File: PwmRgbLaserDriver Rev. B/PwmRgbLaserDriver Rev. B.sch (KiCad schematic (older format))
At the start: 55 parts, among them IC1 ADA4817-1ARDZ, IC2 ADA4817-1ARDZ, IC3 ADA4817-1ARDZ, J1 RED_IN, J2 15V, J3 RLO, J4 GREEN_IN, J5 GLO, J6 BLUE_IN, J7 BLO, Q1 Q_NPN_BCE, Q2 Q_NPN_BCE, Q3 Q_NPN_BCE, U1 TPS54331GDR

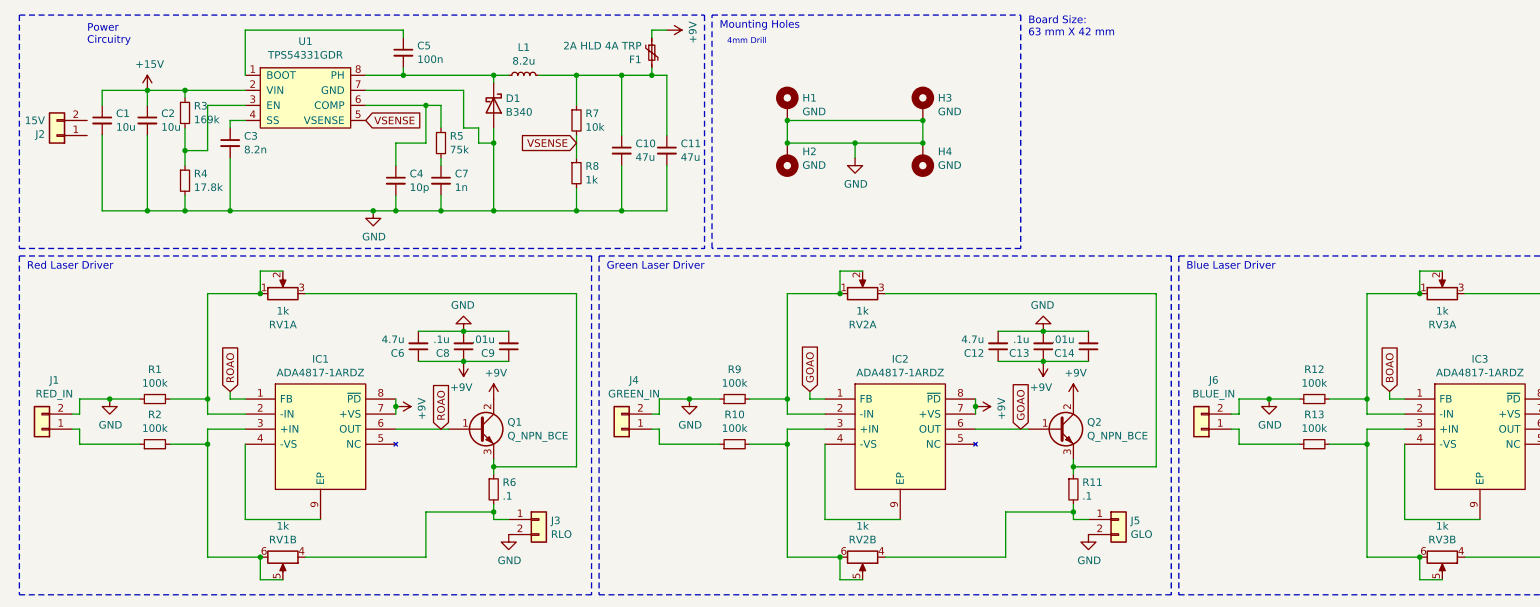
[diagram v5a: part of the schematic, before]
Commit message: Footprints, SMPS Placement
Footprints have now been fully assigned.
The components for the 27W SMPS have been placed.
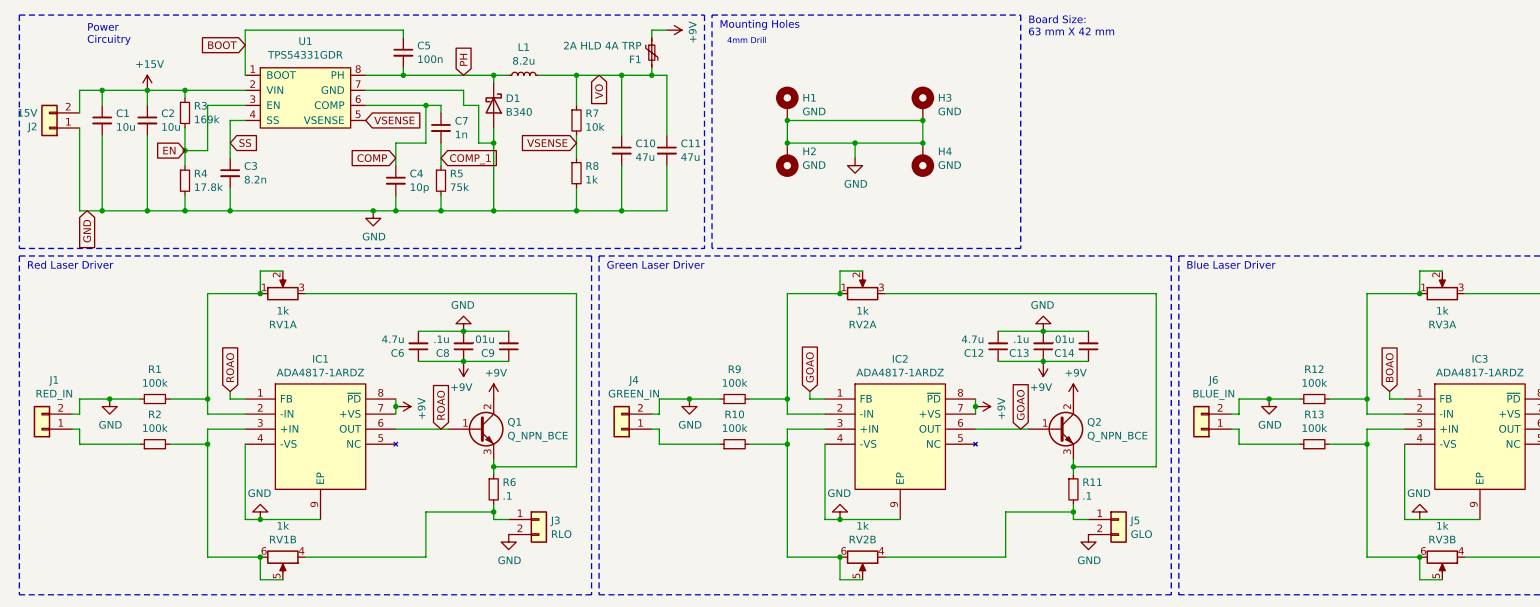
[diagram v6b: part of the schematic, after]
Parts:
- D1: footprint Diode_SMD:D_SMC -> Diode_SMD:D_SMA_Handsoldering
- F1: footprint (none) -> Fuse:Fuse_2920_7451Metric_Pad2.10x5.45mm_HandSolder
- H1, H2, H3, H4: footprint (none) -> SamacSys_Parts:4mm Mounting Hole
- L1: footprint (none) -> SamacSys_Parts:Bourns SRP6540
- Q1, Q2, Q3: footprint (none) -> Package_TO_SOT_SMD:SOT-89-3_Handsoldering
- RV1, RV2, RV3: footprint (none) -> SamacSys_Parts:DualGangPotAmazon
- U1: footprint (none) -> Package_SO:SOIC-8_3.9x4.9mm_P1.27mm
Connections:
- net +15V: now also J2.2 (Pin_2)
- net GND: now also IC1.4 (-VS), IC1.9 (EP), IC2.4 (-VS), IC2.9 (EP), J2.1 (Pin_1), R5.2; no longer C7.2
- net VO: now reaches C10.1, C11.1, F1.2, L1.2, R7.1
- net BOOT: now reaches C5.1, U1.1 (BOOT)
- net EN: now reaches R3.2, R4.1, U1.3 (EN)
- net SS: now reaches C3.1, U1.4 (SS)
- net COMP: now reaches C4.1, U1.6 (COMP)
- net COMP: now also C7.1; no longer R5.1
- net PH: now reaches C5.2, D1.1 (K), L1.1, U1.8 (PH)
- new net COMP_1: C7.2, R5.1
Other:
- moved on the sheet: C3, C7, J2, R5
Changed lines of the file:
@@
 F 0 "Q1" H 3741 3296 50  0000 L CNN
 F 1 "Q_NPN_BCE" H 3741 3205 50  0000 L CNN
-F 2 "" H 3750 3350 50  0001 C CNN
+F 2 "Package_TO_SOT_SMD:SOT-89-3_Handsoldering" H 3750 3350 50  0001 C CNN
 F 3 "~" H 3550 3250 50  0001 C CNN
 	1    3550 3250
@@
 F 0 "RV1" V 2043 2350 50  0000 C CNN
 F 1 "1k" V 2134 2350 50  0000 C CNN
-F 2 "" H 2250 2350 50  0001 C CNN
+F 2 "SamacSys_Parts:DualGangPotAmazon" H 2250 2350 50  0001 C CNN
 F 3 "~" H 2250 2350 50  0001 C CNN
 	1    2250 2350
@@
 F 0 "RV1" V 2135 4100 50  0000 C CNN
 F 1 "1k" V 2044 4100 50  0000 C CNN
-F 2 "" H 2250 4100 50  0001 C CNN
+F 2 "SamacSys_Parts:DualGangPotAmazon" H 2250 4100 50  0001 C CNN
 F 3 "~" H 2250 4100 50  0001 C CNN
 	2    2250 4100
@@
 	2000 3350 2000 3850
 Wire Wire Line
-	2000 3850 2500 3850
+	2000 3850 2100 3850
 Wire Wire Line
 	2100 2350 2100 2200
@@
 F 0 "Q2" H 7591 3296 50  0000 L CNN
 F 1 "Q_NPN_BCE" H 7591 3205 50  0000 L CNN
-F 2 "" H 7600 3350 50  0001 C CNN
+F 2 "Package_TO_SOT_SMD:SOT-89-3_Handsoldering" H 7600 3350 50  0001 C CNN
 F 3 "~" H 7400 3250 50  0001 C CNN
 	1    7400 3250
@@
 F 0 "RV2" V 5893 2350 50  0000 C CNN
 F 1 "1k" V 5984 2350 50  0000 C CNN
-F 2 "" H 6100 2350 50  0001 C CNN
+F 2 "SamacSys_Parts:DualGangPotAmazon" H 6100 2350 50  0001 C CNN
 F 3 "~" H 6100 2350 50  0001 C CNN
 	1    6100 2350
@@
 F 0 "RV2" V 5985 4100 50  0000 C CNN
 F 1 "1k" V 5894 4100 50  0000 C CNN
-F 2 "" H 6100 4100 50  0001 C CNN
+F 2 "SamacSys_Parts:DualGangPotAmazon" H 6100 4100 50  0001 C CNN
 F 3 "~" H 6100 4100 50  0001 C CNN
 	2    6100 4100
@@
 	5850 3350 5850 3850
 Wire Wire Line
-	5850 3850 6350 3850
+	5850 3850 5950 3850
 Wire Wire Line
 	5950 2350 5950 2200
@@
 F 0 "Q3" H 11441 3296 50  0000 L CNN
 F 1 "Q_NPN_BCE" H 11441 3205 50  0000 L CNN
-F 2 "" H 11450 3350 50  0001 C CNN
+F 2 "Package_TO_SOT_SMD:SOT-89-3_Handsoldering" H 11450 3350 50  0001 C CNN
 F 3 "~" H 11250 3250 50  0001 C CNN
 	1    11250 3250
@@
 F 0 "RV3" V 9743 2350 50  0000 C CNN
 F 1 "1k" V 9834 2350 50  0000 C CNN
-F 2 "" H 9950 2350 50  0001 C CNN
+F 2 "SamacSys_Parts:DualGangPotAmazon" H 9950 2350 50  0001 C CNN
 F 3 "~" H 9950 2350 50  0001 C CNN
 	1    9950 2350
@@
 F 0 "RV3" V 9835 4100 50  0000 C CNN
 F 1 "1k" V 9744 4100 50  0000 C CNN
-F 2 "" H 9950 4100 50  0001 C CNN
+F 2 "SamacSys_Parts:DualGangPotAmazon" H 9950 4100 50  0001 C CNN
 F 3 "~" H 9950 4100 50  0001 C CNN
 	2    9950 4100
@@
 L Connector_Generic:Conn_01x02 J2
 U 1 1 60DD581B
-P 750 1300
-F 0 "J2" H 830 1292 50  0000 L CNN
-F 1 "15V" H 830 1201 50  0000 L CNN
-F 2 "Connector_PinHeader_2.54mm:PinHeader_1x02_P2.54mm_Vertical" H 750 1300 50  0001 C CNN
-F 3 "~" H 750 1300 50  0001 C CNN
-	1    750  1300
+P 700 1250
+F 0 "J2" H 780 1242 50  0000 L CNN
+F 1 "15V" H 780 1151 50  0000 L CNN
+F 2 "Connector_PinHeader_2.54mm:PinHeader_1x02_P2.54mm_Vertical" H 700 1250 50  0001 C CNN
+F 3 "~" H 700 1250 50  0001 C CNN
+	1    700  1250
 	-1   0    0    1
 $EndComp
@@
 F 0 "F1" H 4632 704 50  0000 R CNN
 F 1 "2A HLD 4A TRP" H 4632 795 50  0000 R CNN
-F 2 "" H 4750 550 50  0001 L CNN
+F 2 "Fuse:Fuse_2920_7451Metric_Pad2.10x5.45mm_HandSolder" H 4750 550 50  0001 L CNN
 F 3 "~" H 4700 750 50  0001 C CNN
 	1    4700 750
@@
 Wire Wire Line
 	1050 1000 1350 1000
-Wire Wire Line
-	1600 1800 1900 1800
 Connection ~ 1600 1800
 Wire Wire Line
@@
 Wire Wire Line
 	1350 1300 1350 1800
-Connection ~ 1900 1800
 Wire Wire Line
 	1050 1800 1350 1800
@@
 	3550 1350 3650 1350
 Wire Wire Line
-	3550 1250 3550 1350
-Wire Wire Line
-	3450 1250 3550 1250
-Wire Wire Line
-	3450 1000 3450 1250
-Wire Wire Line
 	2800 1000 3450 1000
 Connection ~ 3300 1800
@@
 Wire Wire Line
 	3300 1800 3300 1700
-Wire Wire Line
-	1900 1800 2850 1800
-Wire Wire Line
-	1900 1450 1900 1800
 Connection ~ 3200 1100
 Wire Wire Line
@@
 VSENSE
 Wire Wire Line
-	3300 1100 3300 1250
-Wire Wire Line
-	1900 1200 1900 1250
-Wire Wire Line
 	2000 1200 1900 1200
-Wire Wire Line
-	3300 1500 3300 1450
 $Comp
 L Device:R_Small R5
 U 1 1 60FB31FB
-P 3300 1350
-F 0 "R5" H 3359 1396 50  0000 L CNN
-F 1 "75k" H 3359 1305 50  0000 L CNN
-F 2 "Resistor_SMD:R_0402_1005Metric_Pad0.72x0.64mm_HandSolder" H 3300 1350 50  0001 C CNN
-F 3 "~" H 3300 1350 50  0001 C CNN
-	1    3300 1350
+P 3300 1600
+F 0 "R5" H 3359 1646 50  0000 L CNN
+F 1 "75k" H 3359 1555 50  0000 L CNN
+F 2 "Resistor_SMD:R_0402_1005Metric_Pad0.72x0.64mm_HandSolder" H 3300 1600 50  0001 C CNN
+F 3 "~" H 3300 1600 50  0001 C CNN
+	1    3300 1600
 	1    0    0    -1
 $EndComp
@@
 F 0 "L1" V 4035 900 50  0000 C CNN
 F 1 "8.2u" V 3944 900 50  0000 C CNN
-F 2 "" H 3850 900 50  0001 C CNN
+F 2 "SamacSys_Parts:Bourns SRP6540" H 3850 900 50  0001 C CNN
 F 3 "~" H 3850 900 50  0001 C CNN
 	1    3850 900
@@
 L Device:C_Small C3
 U 1 1 60F5E795
-P 1900 1350
-F 0 "C3" H 1992 1396 50  0000 L CNN
-F 1 "8.2n" H 1992 1305 50  0000 L CNN
-F 2 "Capacitor_SMD:C_0402_1005Metric_Pad0.74x0.62mm_HandSolder" H 1900 1350 50  0001 C CNN
-F 3 "~" H 1900 1350 50  0001 C CNN
-	1    1900 1350
+P 1900 1550
+F 0 "C3" H 1992 1596 50  0000 L CNN
+F 1 "8.2n" H 1992 1505 50  0000 L CNN
+F 2 "Capacitor_SMD:C_0402_1005Metric_Pad0.74x0.62mm_HandSolder" H 1900 1550 50  0001 C CNN
+F 3 "~" H 1900 1550 50  0001 C CNN
+	1    1900 1550
 	1    0    0    -1
 $EndComp
@@
 L Device:C_Small C7
 U 1 1 60F5ACE1
-P 3300 1600
-F 0 "C7" H 3392 1646 50  0000 L CNN
-F 1 "1n" H 3392 1555 50  0000 L CNN
-F 2 "Capacitor_SMD:C_0402_1005Metric_Pad0.74x0.62mm_HandSolder" H 3300 1600 50  0001 C CNN
-F 3 "~" H 3300 1600 50  0001 C CNN
-	1    3300 1600
+P 3300 1250
+F 0 "C7" H 3392 1296 50  0000 L CNN
+F 1 "1n" H 3392 1205 50  0000 L CNN
+F 2 "Capacitor_SMD:C_0402_1005Metric_Pad0.74x0.62mm_HandSolder" H 3300 1250 50  0001 C CNN
+F 3 "~" H 3300 1250 50  0001 C CNN
+	1    3300 1250
 	1    0    0    -1
 $EndComp
@@
 F 0 "D1" V 3604 1180 50  0000 L CNN
 F 1 "B340" V 3695 1180 50  0000 L CNN
-F 2 "Diode_SMD:D_SMC" H 3650 925 50  0001 C CNN
+F 2 "Diode_SMD:D_SMA_Handsoldering" H 3650 925 50  0001 C CNN
 F 3 "http://www.jameco.com/Jameco/Products/ProdDS/1538777.pdf" H 3650 1100 50  0001 C CNN
 	1    3650 1100
@@
 F 0 "U1" H 2400 625 50  0000 C CNN
 F 1 "TPS54331GDR" H 2400 534 50  0000 C CNN
-F 2 "" H 2400 500 50  0001 C CNN
+F 2 "Package_SO:SOIC-8_3.9x4.9mm_P1.27mm" H 2400 500 50  0001 C CNN
 F 3 "" H 2400 500 50  0001 C CNN
 	1    3150 650
@@
 F 0 "H1" H 5700 1149 50  0000 L CNN
 F 1 "GND" H 5700 1058 50  0000 L CNN
-F 2 "" H 5600 1100 50  0001 C CNN
+F 2 "SamacSys_Parts:4mm Mounting Hole" H 5600 1100 50  0001 C CNN
 F 3 "~" H 5600 1100 50  0001 C CNN
 	1    5600 1100
@@
 F 0 "H3" H 6600 1149 50  0000 L CNN
 F 1 "GND" H 6600 1058 50  0000 L CNN
-F 2 "" H 6500 1100 50  0001 C CNN
+F 2 "SamacSys_Parts:4mm Mounting Hole" H 6500 1100 50  0001 C CNN
 F 3 "~" H 6500 1100 50  0001 C CNN
 	1    6500 1100
@@
 F 0 "H4" H 6400 1407 50  0000 R CNN
 F 1 "GND" H 6400 1498 50  0000 R CNN
-F 2 "" H 6500 1450 50  0001 C CNN
+F 2 "SamacSys_Parts:4mm Mounting Hole" H 6500 1450 50  0001 C CNN
 F 3 "~" H 6500 1450 50  0001 C CNN
 	1    6500 1450
@@
 F 0 "H2" H 5500 1407 50  0000 R CNN
 F 1 "GND" H 5500 1498 50  0000 R CNN
-F 2 "" H 5600 1450 50  0001 C CNN
+F 2 "SamacSys_Parts:4mm Mounting Hole" H 5600 1450 50  0001 C CNN
 F 3 "~" H 5600 1450 50  0001 C CNN
 	1    5600 1450
@@
 Text Notes 5200 700  0    39   ~ 0
 4mm Drill
+Wire Wire Line
+	900  1150 900  1000
+Wire Wire Line
+	900  1000 1050 1000
+Connection ~ 1050 1000
+Wire Wire Line
+	900  1250 900  1800
+Wire Wire Line
+	900  1800 1050 1800
+Connection ~ 1050 1800
+Text GLabel 950  1800 3    50   Input ~ 0
+GND
+Text GLabel 4350 900  3    50   Input ~ 0
+VO
+Text GLabel 3450 900  1    50   Input ~ 0
+PH
+Text GLabel 3000 1450 0    50   Input ~ 0
+COMP
+Text GLabel 1600 1400 0    50   Input ~ 0
+EN
+Wire Wire Line
+	1600 1800 1900 1800
+Wire Wire Line
+	1900 1650 1900 1800
+Connection ~ 1900 1800
+Wire Wire Line
+	1900 1800 2850 1800
+Wire Wire Line
+	1900 1200 1900 1450
+Text GLabel 1900 1350 2    50   Input ~ 0
+SS
+Text GLabel 2000 700  0    50   Input ~ 0
+BOOT
+Wire Wire Line
+	3450 1000 3450 1100
+Wire Wire Line
+	3450 1100 3550 1100
+Wire Wire Line
+	3550 1100 3550 1350
+Wire Wire Line
+	3300 1350 3300 1500
+Wire Wire Line
+	3300 1150 3300 1100
+Text GLabel 3300 1450 2    50   Input ~ 0
+COMP_1
+$Comp
+L power:GND #PWR?
+U 1 1 60F58E09
+P 9800 3850
+F 0 "#PWR?" H 9800 3600 50  0001 C CNN
+F 1 "GND" H 9805 3677 50  0000 C CNN
+F 2 "" H 9800 3850 50  0001 C CNN
+F 3 "" H 9800 3850 50  0001 C CNN
+	1    9800 3850
+	-1   0    0    1
+$EndComp
+$Comp
+L power:GND #PWR?
+U 1 1 60F64D0D
+P 5950 3850
+F 0 "#PWR?" H 5950 3600 50  0001 C CNN
+F 1 "GND" H 5955 3677 50  0000 C CNN
+F 2 "" H 5950 3850 50  0001 C CNN
+F 3 "" H 5950 3850 50  0001 C CNN
+	1    5950 3850
+	-1   0    0    1
+$EndComp
+Connection ~ 5950 3850
+Wire Wire Line
+	5950 3850 6350 3850
+$Comp
+L power:GND #PWR?
+U 1 1 60F66A16
+P 2100 3850
+F 0 "#PWR?" H 2100 3600 50  0001 C CNN
+F 1 "GND" H 2105 3677 50  0000 C CNN
+F 2 "" H 2100 3850 50  0001 C CNN
+F 3 "" H 2100 3850 50  0001 C CNN
+	1    2100 3850
+	-1   0    0    1
+$EndComp
+Connection ~ 2100 3850
+Wire Wire Line
+	2100 3850 2500 3850
 $EndSCHEMATC
